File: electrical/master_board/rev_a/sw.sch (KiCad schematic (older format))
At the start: 0 parts

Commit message: Added spacer mounting holes to schematics and associated PCB's.
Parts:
- added H4: HOLE;M2.5, MountingHole:MountingHole_2.7mm_M2.5, symbol HR2:HOLE;M2.5
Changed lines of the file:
@@
 Comment4 ""
 $EndDescr
+$Comp
+L HR2:HOLE;M2.5 H4
+U 1 1 5F2F7A6B
+P 2650 4450
+F 0 "H4" H 2600 4500 60  0000 L CNN
+F 1 "HOLE;M2.5" H 2450 4400 60  0000 L CNN
+F 2 "MountingHole:MountingHole_2.7mm_M2.5" H 2850 4500 60  0001 L CNN
+F 3 "M2.5 Mounting Hole" H 2850 4300 60  0001 L CNN
+	1    2650 4450
+	1    0    0    -1
+$EndComp
 $EndSCHEMATC

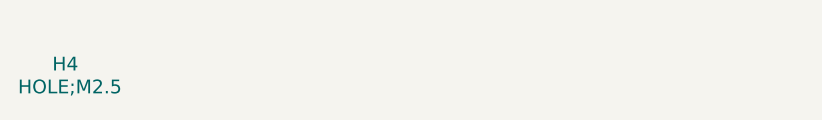
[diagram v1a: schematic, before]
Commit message: Added LED's to the PCB's.
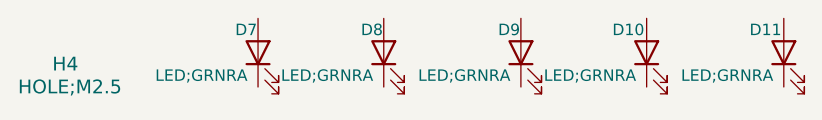
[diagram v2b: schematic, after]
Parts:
- added D10, D11, D7, D8, D9: LED;GRNRA, HR2:LED_GRNRA, symbol Device:LED
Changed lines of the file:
@@
 	1    0    0    -1
 $EndComp
+$Comp
+L Device:LED D7
+U 1 1 5F30BFB1
+P 3500 4350
+F 0 "D7" V 3600 4450 50  0000 R CNN
+F 1 "LED;GRNRA" V 3400 4800 50  0000 R CNN
+F 2 "HR2:LED_GRNRA" H 3500 4350 50  0001 C CNN
+F 3 "~" H 3500 4350 50  0001 C CNN
+	1    3500 4350
+	0    -1   -1   0
+$EndComp
+$Comp
+L Device:LED D8
+U 1 1 5F30CB7A
+P 4050 4350
+F 0 "D8" V 4150 4450 50  0000 R CNN
+F 1 "LED;GRNRA" V 3950 4800 50  0000 R CNN
+F 2 "HR2:LED_GRNRA" H 4050 4350 50  0001 C CNN
+F 3 "~" H 4050 4350 50  0001 C CNN
+	1    4050 4350
+	0    -1   -1   0
+$EndComp
+$Comp
+L Device:LED D9
+U 1 1 5F30CF88
+P 4650 4350
+F 0 "D9" V 4750 4450 50  0000 R CNN
+F 1 "LED;GRNRA" V 4550 4800 50  0000 R CNN
+F 2 "HR2:LED_GRNRA" H 4650 4350 50  0001 C CNN
+F 3 "~" H 4650 4350 50  0001 C CNN
+	1    4650 4350
+	0    -1   -1   0
+$EndComp
+$Comp
+L Device:LED D10
+U 1 1 5F30CF92
+P 5200 4350
+F 0 "D10" V 5300 4500 50  0000 R CNN
+F 1 "LED;GRNRA" V 5100 4800 50  0000 R CNN
+F 2 "HR2:LED_GRNRA" H 5200 4350 50  0001 C CNN
+F 3 "~" H 5200 4350 50  0001 C CNN
+	1    5200 4350
+	0    -1   -1   0
+$EndComp
+$Comp
+L Device:LED D11
+U 1 1 5F30EB24
+P 5800 4350
+F 0 "D11" V 5900 4500 50  0000 R CNN
+F 1 "LED;GRNRA" V 5700 4800 50  0000 R CNN
+F 2 "HR2:LED_GRNRA" H 5800 4350 50  0001 C CNN
+F 3 "~" H 5800 4350 50  0001 C CNN
+	1    5800 4350
+	0    -1   -1   0
+$EndComp
 $EndSCHEMATC

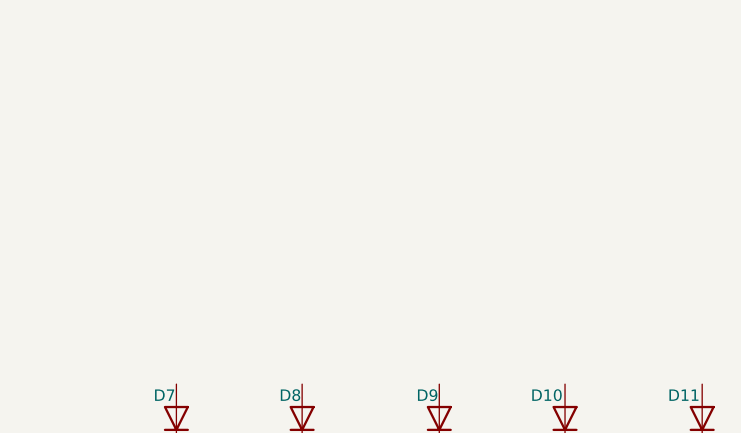
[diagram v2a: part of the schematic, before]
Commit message: Got Bridge connectors installed on PCB's. Tweaking still required.
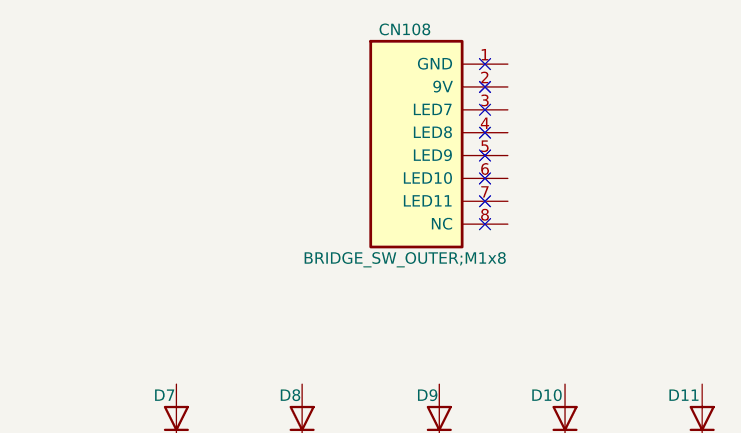
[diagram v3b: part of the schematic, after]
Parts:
- added CN108: BRIDGE_SW_OUTER;M1x8, HR2:BRIDGE_SW_OUTER_M1x8, symbol HR2:BRIDGE_SW_OUTER;M1x8
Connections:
- no-connect marks 0 -> 8
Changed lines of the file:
@@
 	0    -1   -1   0
 $EndComp
+$Comp
+L HR2:BRIDGE_SW_OUTER;M1x8 CN108
+U 1 1 5F387C15
+P 4150 2800
+F 0 "CN108" H 4500 2950 50  0000 C CNN
+F 1 "BRIDGE_SW_OUTER;M1x8" H 4500 1950 50  0000 C CNN
+F 2 "HR2:BRIDGE_SW_OUTER_M1x8" H 4350 2850 60  0001 L CNN
+F 3 "" H 4350 2650 60  0001 L CNN
+F 4 "SW Outer Bridge Connector" H 4350 2550 60  0001 L CNN "Field5"
+	1    4150 2800
+	1    0    0    -1
+$EndComp
+NoConn ~ 4850 2800
+NoConn ~ 4850 2900
+NoConn ~ 4850 3000
+NoConn ~ 4850 3100
+NoConn ~ 4850 3200
+NoConn ~ 4850 3300
+NoConn ~ 4850 3400
+NoConn ~ 4850 3500
 $EndSCHEMATC

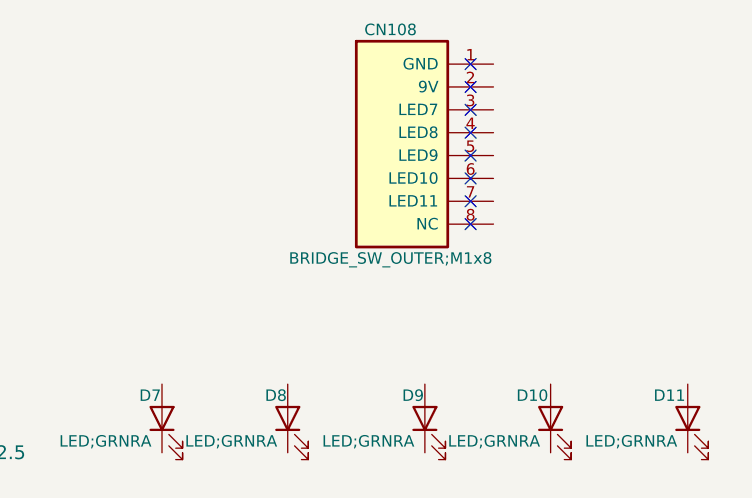
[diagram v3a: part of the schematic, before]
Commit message: Started working on zones. (Added zone to sw.pro)
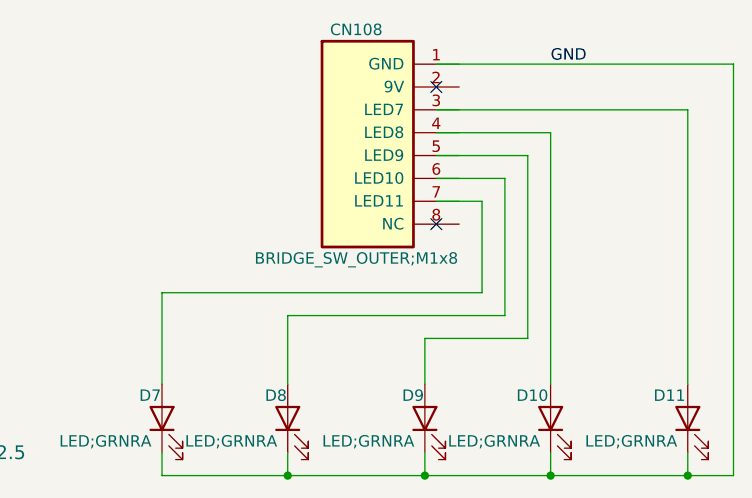
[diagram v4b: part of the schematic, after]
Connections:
- net labels added: GND
- wire segments 0 -> 28
- no-connect marks 8 -> 2
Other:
- moved on the sheet: CN108
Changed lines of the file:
@@
 L HR2:BRIDGE_SW_OUTER;M1x8 CN108
 U 1 1 5F387C15
-P 4150 2800
-F 0 "CN108" H 4500 2950 50  0000 C CNN
-F 1 "BRIDGE_SW_OUTER;M1x8" H 4500 1950 50  0000 C CNN
-F 2 "HR2:BRIDGE_SW_OUTER_M1x8" H 4350 2850 60  0001 L CNN
-F 3 "" H 4350 2650 60  0001 L CNN
-F 4 "SW Outer Bridge Connector" H 4350 2550 60  0001 L CNN "Field5"
-	1    4150 2800
+P 4000 2800
+F 0 "CN108" H 4350 2950 50  0000 C CNN
+F 1 "BRIDGE_SW_OUTER;M1x8" H 4350 1950 50  0000 C CNN
+F 2 "HR2:BRIDGE_SW_OUTER_M1x8" H 4200 2850 60  0001 L CNN
+F 3 "" H 4200 2650 60  0001 L CNN
+F 4 "SW Outer Bridge Connector" H 4200 2550 60  0001 L CNN "Field5"
+	1    4000 2800
 	1    0    0    -1
 $EndComp
-NoConn ~ 4850 2800
-NoConn ~ 4850 2900
-NoConn ~ 4850 3000
-NoConn ~ 4850 3100
-NoConn ~ 4850 3200
-NoConn ~ 4850 3300
-NoConn ~ 4850 3400
-NoConn ~ 4850 3500
+NoConn ~ 4700 2900
+NoConn ~ 4700 3500
+Wire Wire Line
+	3500 4500 3500 4600
+Wire Wire Line
+	3500 4600 4050 4600
+Wire Wire Line
+	5800 4600 5800 4500
+Wire Wire Line
+	4050 4500 4050 4600
+Connection ~ 4050 4600
+Wire Wire Line
+	4050 4600 4650 4600
+Wire Wire Line
+	4650 4500 4650 4600
+Connection ~ 4650 4600
+Wire Wire Line
+	4650 4600 5200 4600
+Wire Wire Line
+	5200 4500 5200 4600
+Connection ~ 5200 4600
+Wire Wire Line
+	5200 4600 5800 4600
+Wire Wire Line
+	5800 4600 6000 4600
+Wire Wire Line
+	6000 4600 6000 2800
+Wire Wire Line
+	6000 2800 4700 2800
+Connection ~ 5800 4600
+Text Label 5200 2800 0    50   ~ 0
+GND
+Wire Wire Line
+	5800 4200 5800 3000
+Wire Wire Line
+	5800 3000 4700 3000
+Wire Wire Line
+	5200 4200 5200 3100
+Wire Wire Line
+	5200 3100 4700 3100
+Wire Wire Line
+	4700 3400 4900 3400
+Wire Wire Line
+	4900 3400 4900 3800
+Wire Wire Line
+	4900 3800 3500 3800
+Wire Wire Line
+	3500 3800 3500 4200
+Wire Wire Line
+	4700 3300 5000 3300
+Wire Wire Line
+	5000 3300 5000 3900
+Wire Wire Line
+	5000 3900 4050 3900
+Wire Wire Line
+	4050 3900 4050 4200
+Wire Wire Line
+	4650 4200 4650 4000
+Wire Wire Line
+	4650 4000 5100 4000
+Wire Wire Line
+	5100 4000 5100 3200
+Wire Wire Line
+	5100 3200 4700 3200
 $EndSCHEMATC

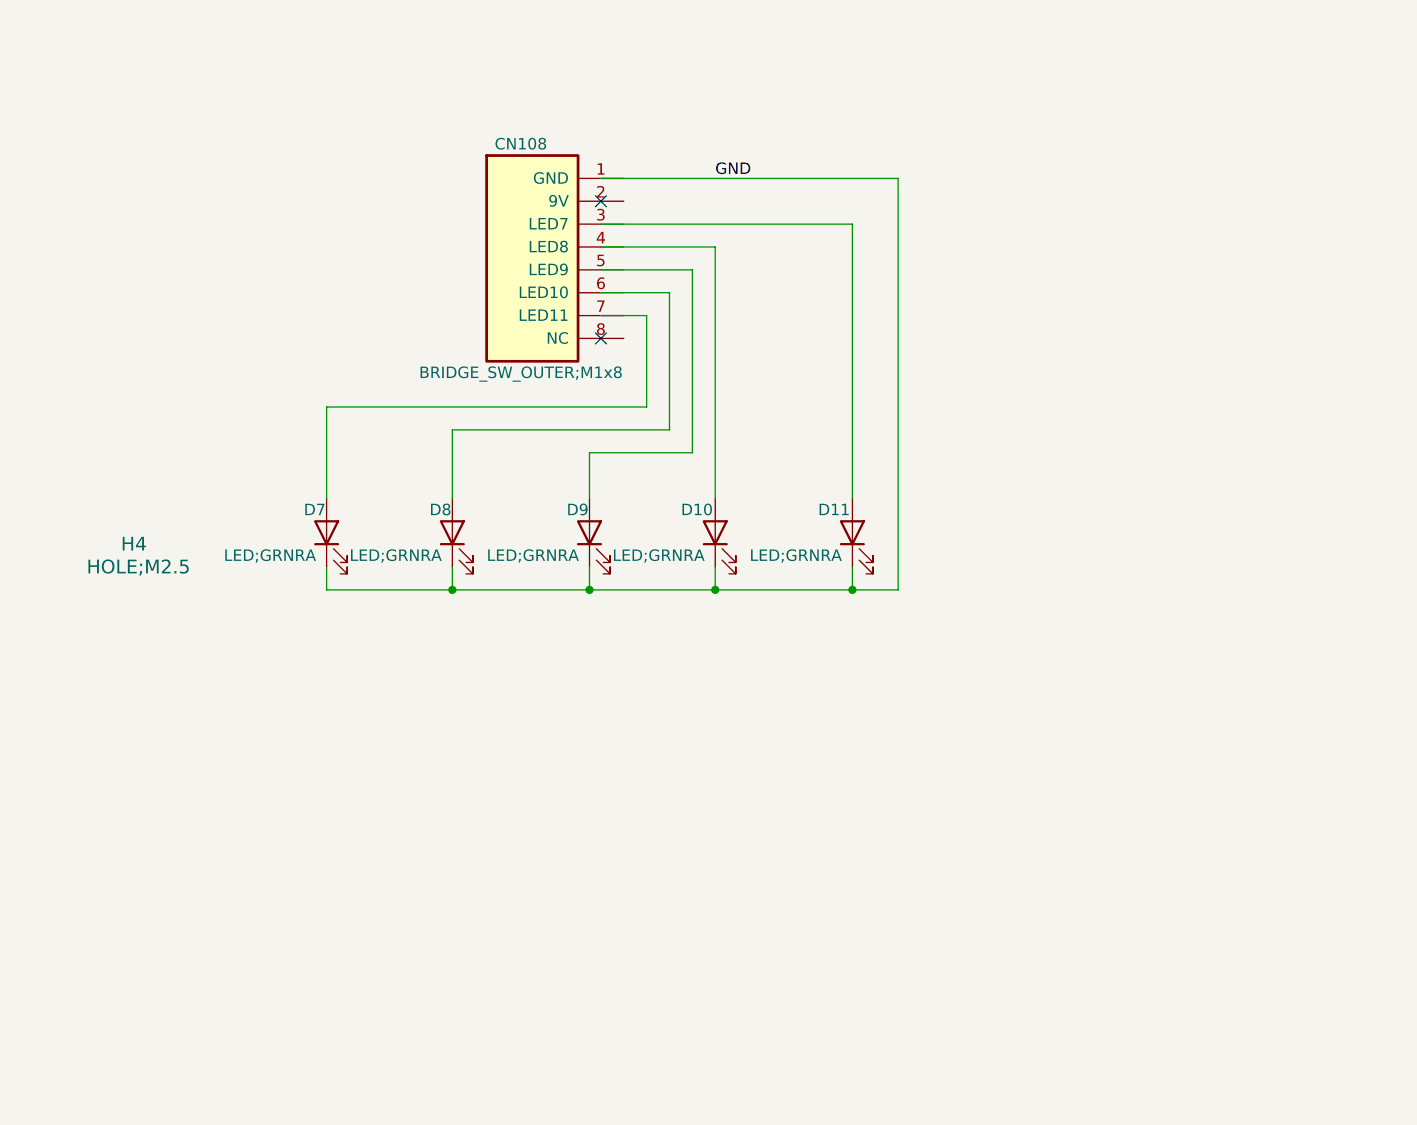
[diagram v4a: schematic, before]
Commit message: Layed out SW PCB.
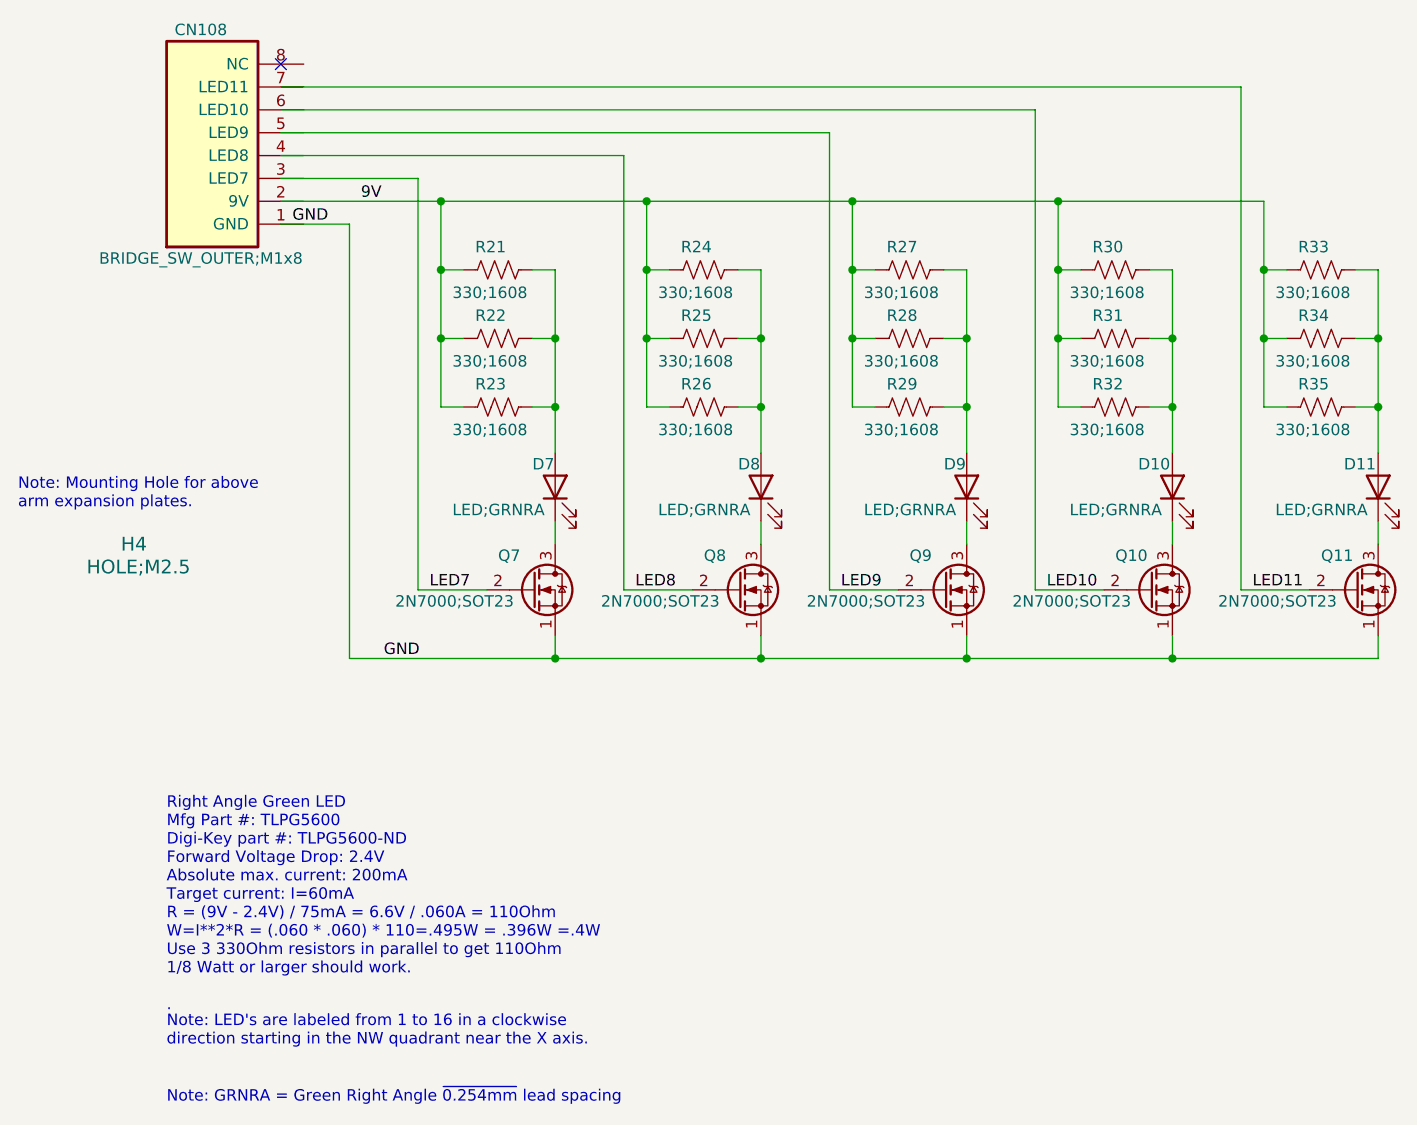
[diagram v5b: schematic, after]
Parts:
- added Q10, Q11, Q7, Q8, Q9: 2N7000;SOT23, Package_TO_SOT_SMD:SOT-23, symbol Transistor_FET:2N7000
- added R21, R22, R23, R24, R25, R26, R27, R28, R29, R30, R31, R32, R33, R34, R35: 330;1608, Resistor_SMD:R_0603_1608Metric, symbol Device:R_US
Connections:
- net labels added: 9V, LED10, LED11, LED7, LED8, LED9
- wire segments 28 -> 97
- no-connect marks 2 -> 1
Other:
- note added: "Note: GRNRA = Green Right Angle ~0.254mm lead spacing"
- note added: "Note: LED's are labeled from 1 to 16 in a clockwise\ndirection starting in the NW quadrant near the X axis."
- note added: "Note: Mounting Hole for above\narm expansion plates."
- note added: "Right Angle Green LED\nMfg Part #: TLPG5600\nDigi-Key part #: TLPG5600-ND\nForward Voltage Drop: 2.4V\nAbsolute max. current: 200mA\nTarget current: I=60mA\nR = (9V - 2.4V) / 75mA = 6.6V / .060A = 110Ohm\nW=I**2*R = (.060 * .060) * 110=.495W = .396W =.4W\nUse 3 330Ohm resistors in parallel to get 110Ohm\n1/8 Watt or larger should work.\n\n.\n"
- moved on the sheet: CN108, D10, D11, D7, D8, D9

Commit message: Preparing to start SE PCB.
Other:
- note added: "Note: GRNRA = Green Right Angle 0.254mm (approx.) lead spacing"
- note removed: "Note: GRNRA = Green Right Angle ~0.254mm lead spacing"
- moved on the sheet: CN108
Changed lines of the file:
@@
 U 1 1 5F2F7A6B
 P 2650 4450
-F 0 "H4" H 2600 4500 60  0000 L CNN
-F 1 "HOLE;M2.5" H 2450 4400 60  0000 L CNN
+F 0 "H4" H 2600 4500 50  0000 L CNN
+F 1 "HOLE;M2.5" H 2450 4400 50  0000 L CNN
 F 2 "MountingHole:MountingHole_2.7mm_M2.5" H 2850 4500 60  0001 L CNN
 F 3 "M2.5 Mounting Hole" H 2850 4300 60  0001 L CNN
@@
 L HR2:BRIDGE_SW_OUTER;M1x8 CN108
 U 1 1 5F387C15
-P 2600 3000
-F 0 "CN108" H 2950 2150 50  0000 C CNN
-F 1 "BRIDGE_SW_OUTER;M1x8" H 2950 3150 50  0000 C CNN
-F 2 "HR2:BRIDGE_SW_OUTER_M1x8" H 2800 3050 60  0001 L CNN
-F 3 "" H 2800 2850 60  0001 L CNN
-F 4 "SW Outer Bridge Connector" H 2800 2750 60  0001 L CNN "Field5"
-	1    2600 3000
+P 2500 3000
+F 0 "CN108" H 2850 2150 50  0000 C CNN
+F 1 "BRIDGE_SW_OUTER;M1x8" H 2850 3150 50  0000 C CNN
+F 2 "HR2:BRIDGE_SW_OUTER_M1x8" H 2700 3050 60  0001 L CNN
+F 3 "" H 2700 2850 60  0001 L CNN
+F 4 "SW Outer Bridge Connector" H 2700 2750 60  0001 L CNN "Field5"
+	1    2500 3000
 	1    0    0    1
 $EndComp
@@
 9V
 Text Notes 2800 6850 0    50   ~ 0
-Note: GRNRA = Green Right Angle ~0.254mm lead spacing
+Note: GRNRA = Green Right Angle 0.254mm (approx.) lead spacing
 Text Notes 2800 6600 0    50   ~ 0
 Note: LED's are labeled from 1 to 16 in a clockwise\ndirection starting in the NW quadrant near the X axis.
